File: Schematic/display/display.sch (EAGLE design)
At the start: 15 parts, among them IC2 74AC11032D, IC3 74HC08D, Q1 FDS6890A, Q2 FDS6890A

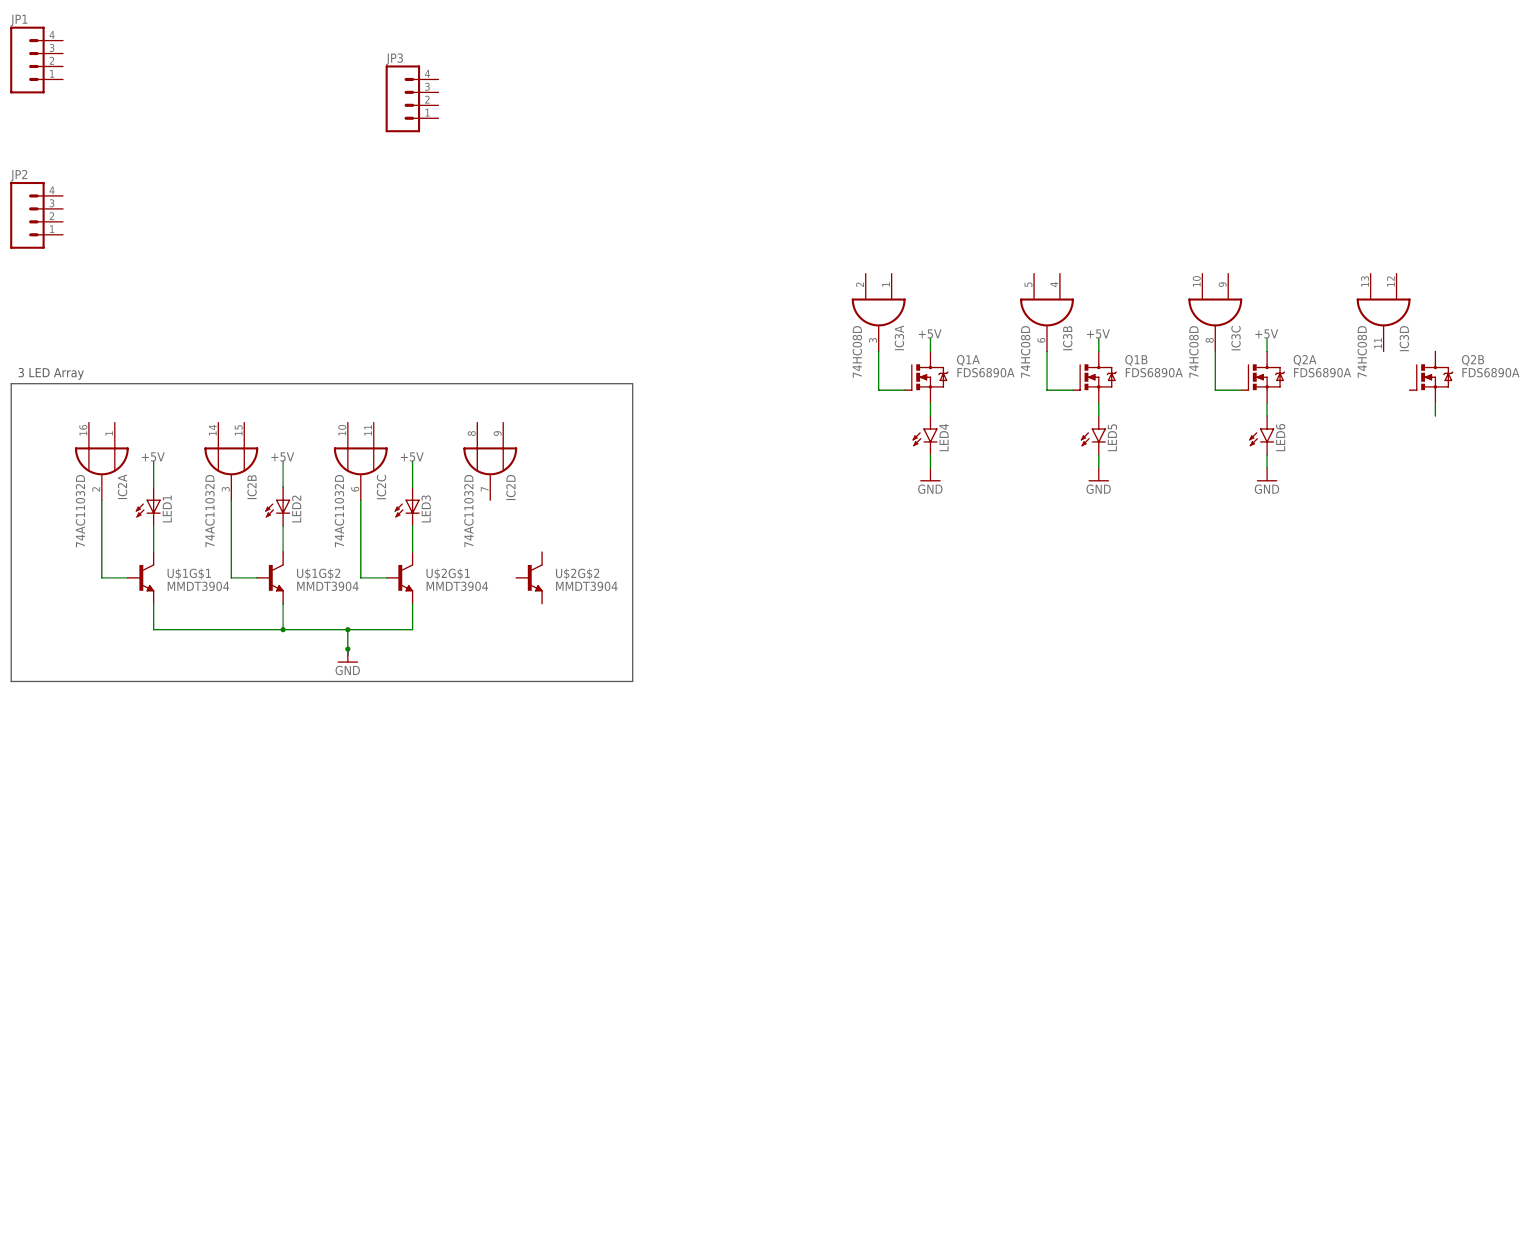
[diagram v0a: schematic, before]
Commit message: Basic layout of display circuit. Componant values and part numbers require update. Still needs interface to main board.
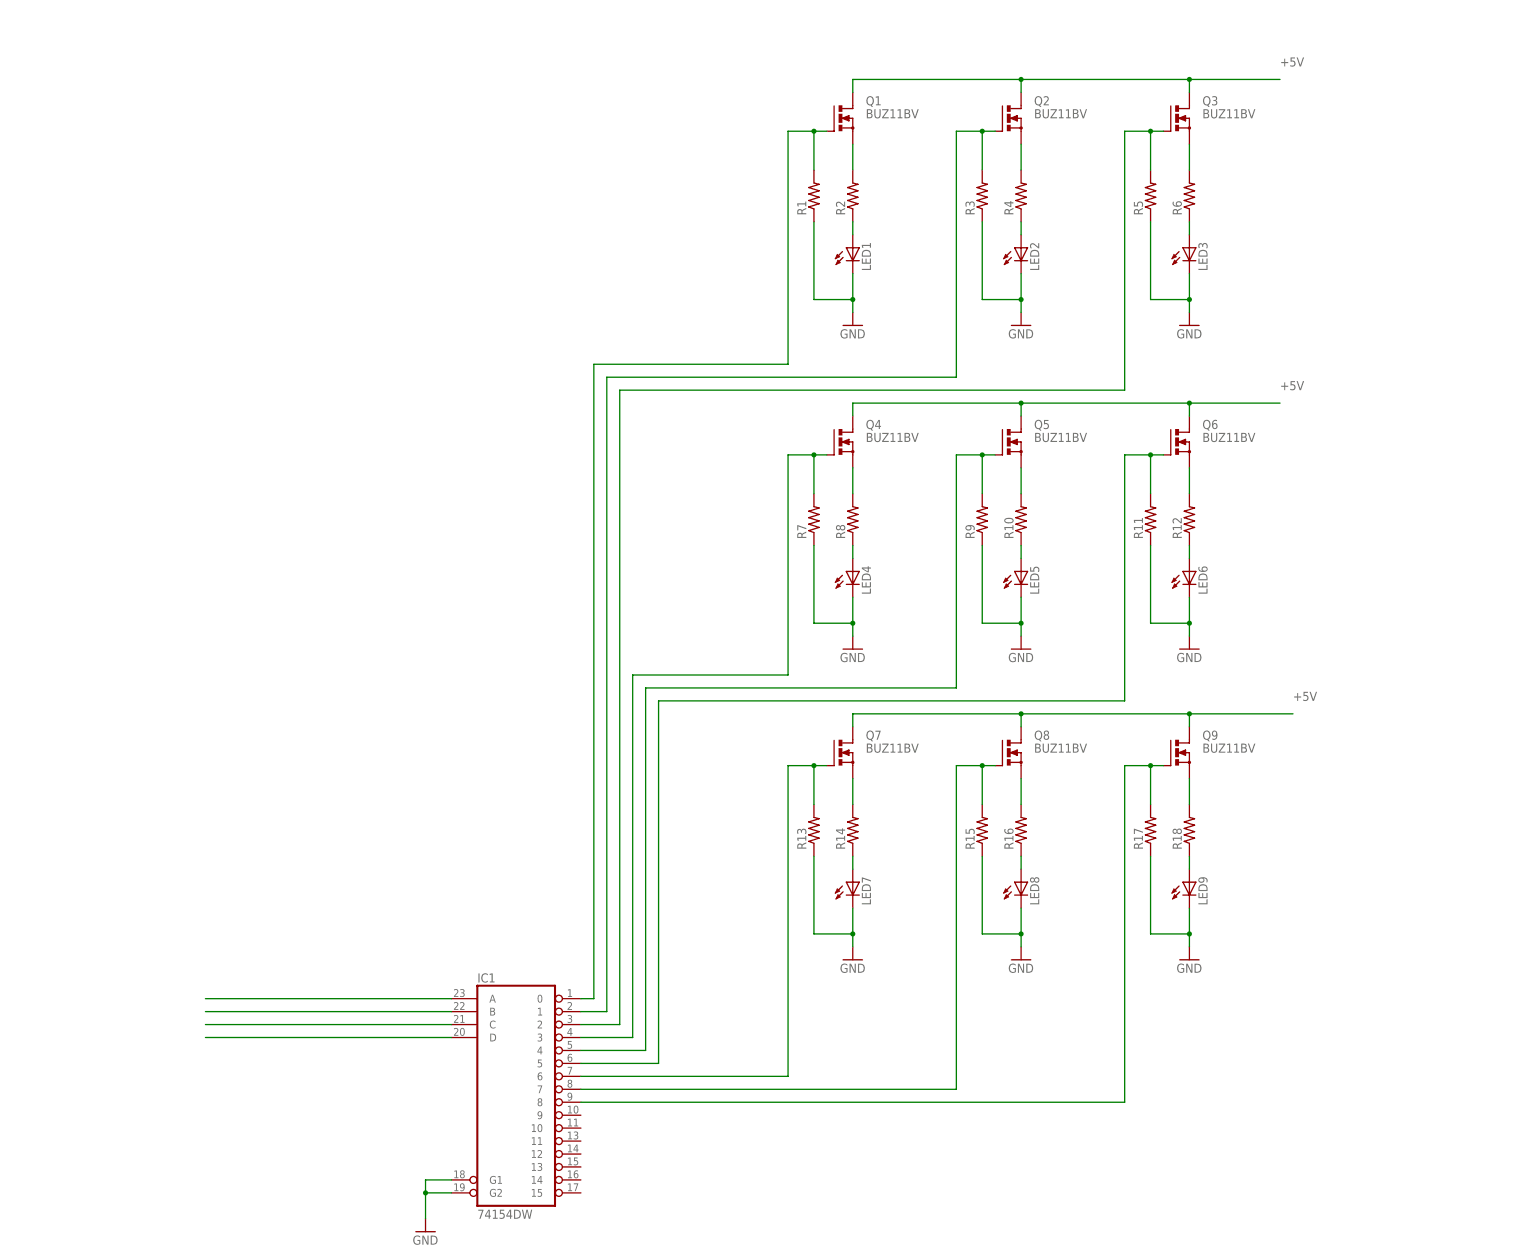
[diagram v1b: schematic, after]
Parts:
- removed IC2: 74AC11032D, 74ac-logic:74AC11032D
- removed IC3: 74HC08D, 74xx-eu:74HC08D
- removed JP1, JP2, JP3: (no value), SparkFun-Connectors:M04JST
- removed U$1, U$2: MMDT3904, SparkFun-DiscreteSemi:TRANSISTOR_NPN2UPMMDT3904
- added IC1: 74154DW, 74xx-us:74154DW
- added LED7, LED8, LED9: (no value), led:LEDSMT1206
- added Q3, Q4, Q5, Q6, Q7, Q8, Q9: BUZ11BV, transistor-power:BUZ11BV
- added R1, R10, R11, R12, R13, R14, R15, R16, R17, R18, R2, R3, R4, R5, R6, R7, R8, R9: (no value), resistor:R-US_M3516
- LED1, LED2, LED3: device led:LED3MM -> led:LEDSMT1206
- LED4, LED5, LED6: device SparkFun-LED:LED-3MM-NO_SILK -> led:LEDSMT1206
- Q1, Q2: value FDS6890A -> BUZ11BV; device transistor-power:FDS6890A -> transistor-power:BUZ11BV
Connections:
- removed net N$10: Q2B.S
- removed net N$11: IC3A.O, Q1A.G
- new net N$14: Q5.S, R10.2
- new net N$15: Q6.S, R12.2
- new net N$16: LED5.A, R10.1
- new net N$17: LED4.A, R8.1
- new net N$20: LED6.A, R12.1
- new net N$21: Q7.S, R14.2
- new net N$24: Q8.S, R16.2
- new net N$26: Q9.S, R18.2
- new net N$27: LED9.A, R18.1
- new net N$28: LED8.A, R16.1
- new net N$29: LED7.A, R14.1
- new net N$36: IC1A.0, Q1.G, R1.2
- new net N$37: IC1A.1, Q2.G, R3.2
- new net N$38: IC1A.2, Q3.G, R5.2
- new net N$39: IC1A.3, Q4.G, R7.2
- new net N$40: IC1A.4, Q5.G, R9.2
- new net N$41: IC1A.5, Q6.G, R11.2
- new net N$42: IC1A.6, Q7.G, R13.2
- new net N$43: IC1A.7, Q8.G, R15.2
- new net N$44: IC1A.8, Q9.G, R17.2
- new net N$45: IC1A.G1, IC1A.G2
- net +5V: now also Q1.D, Q2.D, Q3.D, Q4.D, Q5.D, Q6.D, Q7.D, Q8.D, Q9.D; no longer LED1.A, LED2.A, LED3.A, Q1A.D, Q1B.D, Q2A.D
- net GND: now also LED1.C, LED2.C, LED3.C, LED7.C, LED8.C, LED9.C, R1.1, R11.1, R13.1, R15.1, R17.1, R3.1, R5.1, R7.1, R9.1; no longer U$1G$1.E, U$1G$2.E, U$2G$1.E
- net N$1: now also Q1.S, R2.2; no longer IC2A.O, U$1G$1.B
- net N$12: now also LED2.A, R4.1; no longer IC3B.O, Q1B.G
- net N$13: now also Q4.S, R8.2; no longer IC3C.O, Q2A.G
- net N$2: now also Q2.S, R4.2; no longer IC2B.O, U$1G$2.B
- net N$3: now also Q3.S, R6.2; no longer IC2C.O, U$2G$1.B
- net N$4: now also IC1A.D; no longer LED5.A, Q1B.S
- net N$5: now also IC1A.C; no longer LED1.C, U$1G$1.C
- net N$6: now also IC1A.B; no longer LED4.A, Q1A.S
- net N$7: now also IC1A.A; no longer LED6.A, Q2A.S
- net N$8: now also LED1.A, R2.1; no longer LED2.C, U$1G$2.C
- net N$9: now also LED3.A, R6.1; no longer LED3.C, U$2G$1.C
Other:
- note removed: "3 LED Array"
- moved on the sheet: LED1, LED2, LED3
